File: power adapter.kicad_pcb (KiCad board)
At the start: 2 copper layers, 76.2 x 50.8 mm, 0 parts

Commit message: board started
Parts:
- added C3: T491C106M025AT7280, customfootprints:10uFtantcap, F.Cu at (38.7, 85.6)
- added C4: T491C106M025AT7280, customfootprints:10uFtantcap, F.Cu at (47.2, 99.4)
- added U1: ~, adapterpcblib:Header2x5, F.Cu at (40.4, 91.2)
- added jk1: ~, adapterpcblib:Banana, F.Cu at (81.5, 82.5)
- added jk2: ~, adapterpcblib:Banana, F.Cu at (80.8, 94.0)
- added jk3: ~, adapterpcblib:Banana, F.Cu at (80.0, 105.4)
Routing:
- net GND: track 0.00 -> 81.5 mm
- net -12V: track 0.00 -> 45.3 mm
- net +12V: track 0.00 -> 41.3 mm
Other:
- board size 76.2 x 50.8 mm -> 63.5 x 38.1 mm

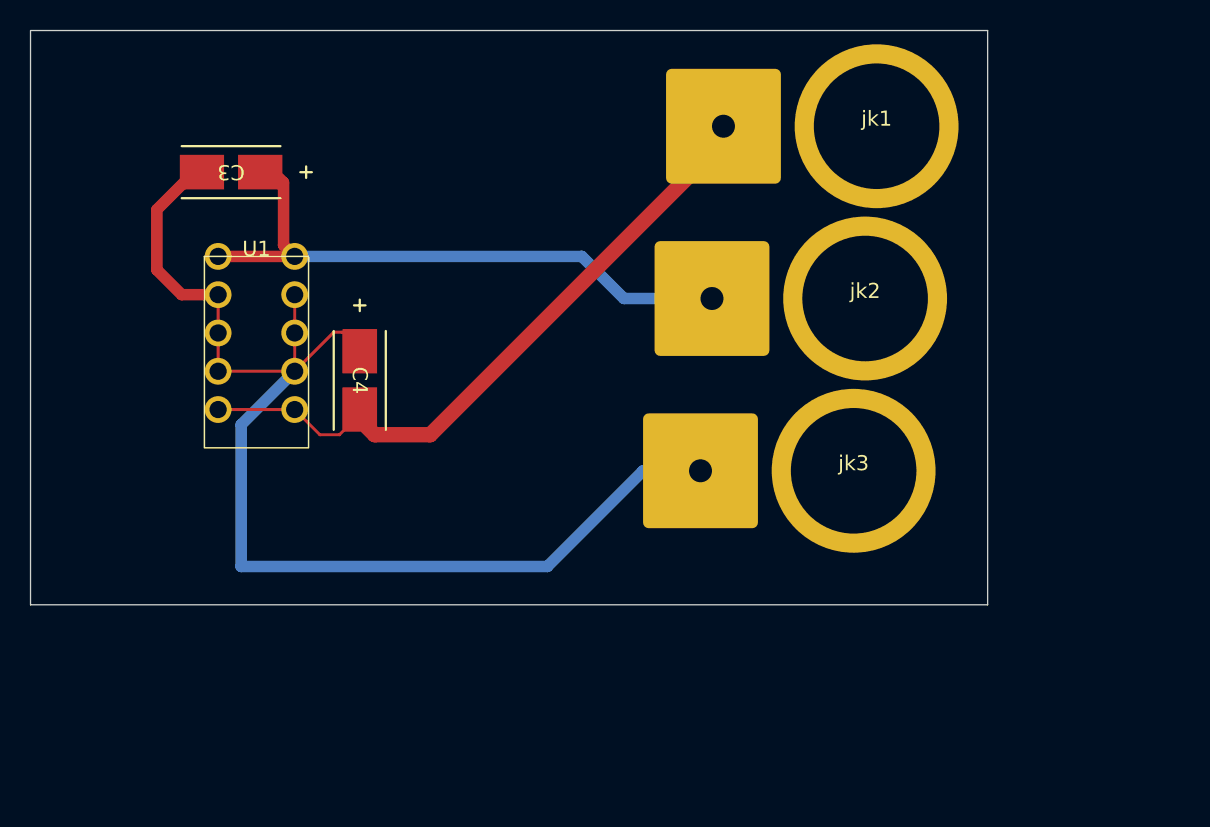
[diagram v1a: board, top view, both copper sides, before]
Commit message: rotated power header
rotated power header anotated schematic, turned on silkscreen layer
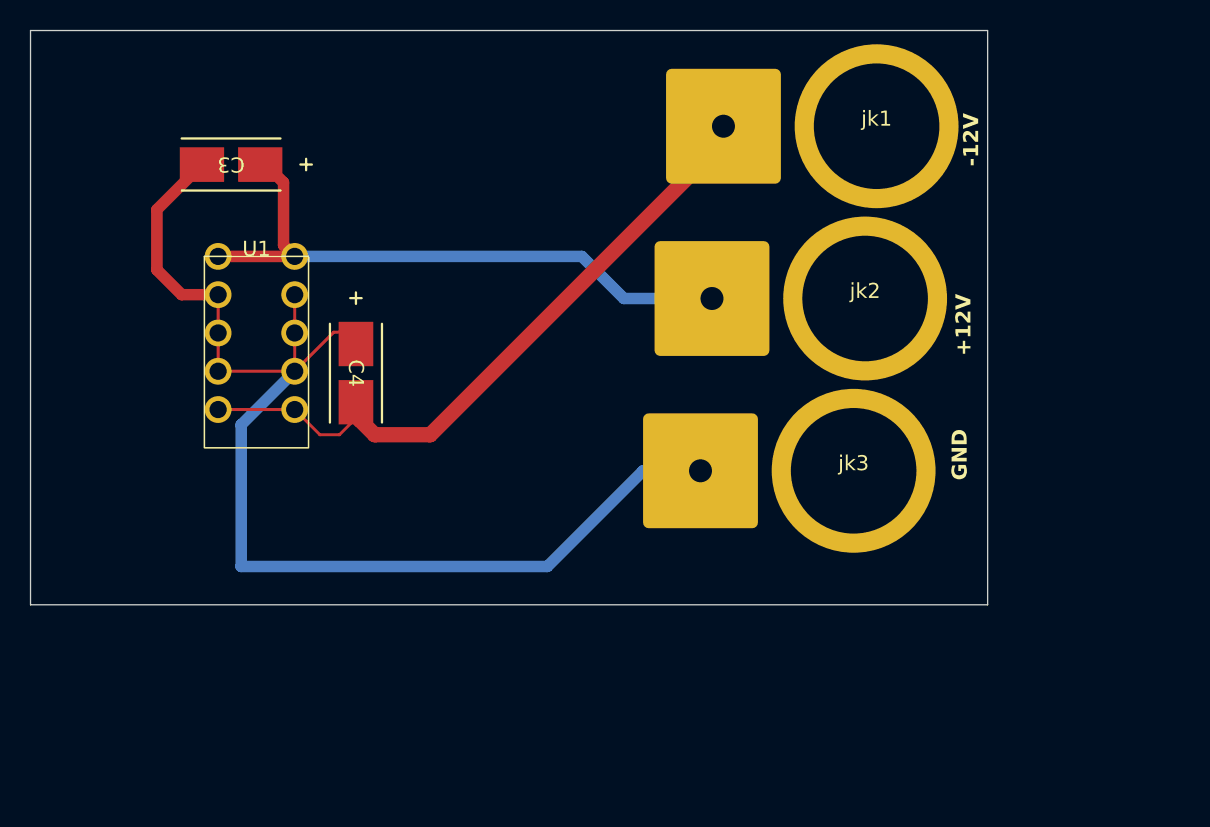
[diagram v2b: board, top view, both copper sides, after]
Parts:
- moved C4 0.54 mm to (47.0, 98.9)
- moved C3 0.51 mm to (38.7, 85.1)
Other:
- board text added: "+12V"
- board text added: "-12V"
- board text added: "GND"

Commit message: added power lanes
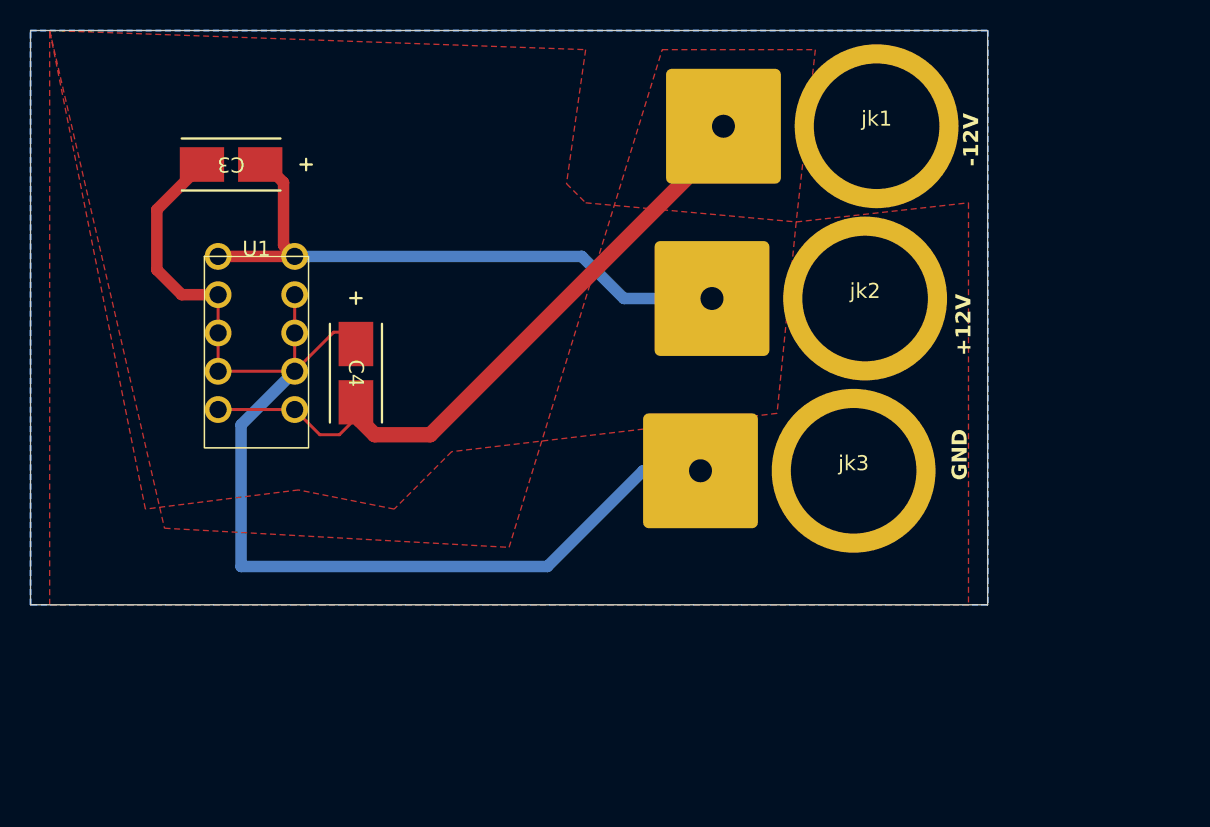
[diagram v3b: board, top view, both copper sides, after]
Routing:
- added copper zone on B.Cu, net (none)
- added copper zone on F.Cu, net +12V
- added copper zone on F.Cu, net -12V
- added copper zone on B.Cu, net GND

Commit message: updateEuroHeader
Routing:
- net GND: track 81.5 -> 82.3 mm, vias 0 -> 1
- removed copper zone on F.Cu, net +12V
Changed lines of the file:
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@@
 		(sheetfile "power adapter.kicad_sch")
 		(attr through_hole)
+		(fp_line
+			(start -4.525 -2.18)
+			(end 3.825 -2.18)
+			(stroke
+				(width 1.016)
+				(type default)
+			)
+			(layer "F.SilkS")
+		)
+		(fp_rect
+			(start -4.72 3.705)
+			(end -3.58 7.275)
+			(stroke
+				(width 0.1)
+				(type solid)
+			)
+			(fill solid)
+			(layer "F.SilkS")
+		)
 		(fp_rect
 			(start -3.45 0)
@@
 			)
 			(fill none)
+			(layer "F.SilkS")
+		)
+		(fp_circle
+			(center -4.37 0.01)
+			(end -3.93 0.01)
+			(stroke
+				(width 0.1)
+				(type solid)
+			)
+			(fill solid)
 			(layer "F.SilkS")
 		)
@@
 	)
 	(segment
-		(start 33.782 88.085492)
-		(end 33.782 92.075)
-		(width 0.762)
-		(layer "F.Cu")
-		(net 1)
-	)
-	(segment
 		(start 36.269492 85.598)
 		(end 36.773408 85.598)
@@
 	)
 	(segment
-		(start 33.782 92.075)
-		(end 35.433 93.726)
-		(width 0.762)
-		(layer "F.Cu")
-		(net 1)
-	)
-	(segment
-		(start 36.269492 85.598)
-		(end 33.782 88.085492)
-		(width 0.762)
-		(layer "F.Cu")
-		(net 1)
-	)
-	(segment
 		(start 45.51849 96.21351)
 		(end 46.084624 96.21351)
@@
 	)
 	(segment
-		(start 35.433 93.726)
-		(end 37.846 93.726)
-		(width 0.762)
+		(start 34.29 87.63)
+		(end 34.29 86.889886)
+		(width 1.016)
+		(layer "F.Cu")
+		(net 1)
+	)
+	(segment
+		(start 34.29 86.889886)
+		(end 36.089886 85.09)
+		(width 1.016)
 		(layer "F.Cu")
 		(net 1)
@@
 		(width 0.2)
 		(layer "F.Cu")
+		(net 1)
+	)
+	(segment
+		(start 36.089886 85.09)
+		(end 36.773408 85.09)
+		(width 1.016)
+		(layer "F.Cu")
+		(net 1)
+	)
+	(via
+		(at 34.29 87.63)
+		(size 0.5)
+		(drill 0.3)
+		(layers "F.Cu" "B.Cu")
 		(net 1)
 	)
@@
 	)
 	(segment
+		(start 35.306 93.726)
+		(end 34.29 92.71)
+		(width 1.016)
+		(layer "B.Cu")
+		(net 1)
+	)
+	(segment
 		(start 66.04 105.41)
 		(end 59.69 111.76)
@@
 	)
 	(segment
+		(start 37.846 93.726)
+		(end 35.306 93.726)
+		(width 1.016)
+		(layer "B.Cu")
+		(net 1)
+	)
+	(segment
 		(start 39.37 102.362)
 		(end 42.926 98.806)
 		(width 0.762)
+		(layer "B.Cu")
+		(net 1)
+	)
+	(segment
+		(start 34.29 92.71)
+		(end 34.29 87.63)
+		(width 1.016)
 		(layer "B.Cu")
 		(net 1)
@@
 	)
 	(zone
-		(net 3)
-		(net_name "+12V")
+		(net 2)
+		(net_name "-12V")
 		(layer "F.Cu")
 		(hatch edge 0.5)
-		(priority 4)
+		(priority 5)
 		(connect_pads
 			(clearance 0.5)
@@
 			(thermal_gap 0.5)
 			(thermal_bridge_width 0.5)
+			(island_removal_mode 1)
+			(island_area_min 9.999999)
 		)
 		(polygon
@@
 		(layer "F.Cu")
 		(hatch edge 0.5)
-		(priority 5)
+		(priority 4)
 		(connect_pads
 			(clearance 0.5)
@@
 		(polygon
 			(pts
-				(xy 26.67 76.2) (xy 34.29 109.22) (xy 57.15 110.49) (xy 67.31 77.47) (xy 77.47 77.47) (xy 76.2 88.9)
+				(xy 26.67 76.2) (xy 34.29 109.22) (xy 48.26 106.68) (xy 67.31 77.47) (xy 76.2 77.47) (xy 76.2 88.9)
 				(xy 87.63 87.63) (xy 87.63 114.3) (xy 26.67 114.3)
 			)
@@
 			(pts
 				(xy 25.4 76.2) (xy 88.9 76.2) (xy 88.9 114.3) (xy 25.4 114.3)
+			)
+		)
+	)
+	(zone
+		(net 1)
+		(net_name "GND")
+		(layer "B.Cu")
+		(hatch edge 0.5)
+		(priority 7)
+		(connect_pads
+			(clearance 0.5)
+		)
+		(min_thickness 0.25)
+		(filled_areas_thickness no)
+		(fill yes
+			(thermal_gap 0.5)
+			(thermal_bridge_width 0.5)
+			(island_removal_mode 1)
+			(island_area_min 9.999998)
+		)
+		(polygon
+			(pts
+				(xy 25.4 114.3) (xy 25.4 76.2) (xy 88.9 76.2) (xy 88.9 114.3)
 			)
 		)
@@
 			(thermal_bridge_width 0.5)
 			(island_removal_mode 1)
-			(island_area_min 9.999999)
+			(island_area_min 9.999998)
 		)
 		(polygon
 			(pts
-				(xy 88.9 76.2) (xy 88.9 114.3) (xy 25.4 114.3) (xy 25.4 76.2)
+				(xy 88.9 76.2) (xy 88.9 114.3) (xy 25.4 114.3)
 			)
 		)
@@
 			)
 		)
+	)
+	(zone
+		(net 1)
+		(net_name "GND")
+		(layer "B.Cu")
+		(hatch edge 0.5)
+		(priority 6)
+		(connect_pads
+			(clearance 0.5)
+		)
+		(min_thickness 0.25)
+		(filled_areas_thickness no)
+		(fill yes
+			(thermal_gap 0.5)
+			(thermal_bridge_width 0.5)
+			(island_removal_mode 1)
+			(island_area_min 9.999998)
+		)
+		(polygon
+			(pts
+				(xy 25.4 76.2) (xy 88.9 76.2) (xy 88.9 114.3) (xy 25.4 114.3)
+			)
+		)

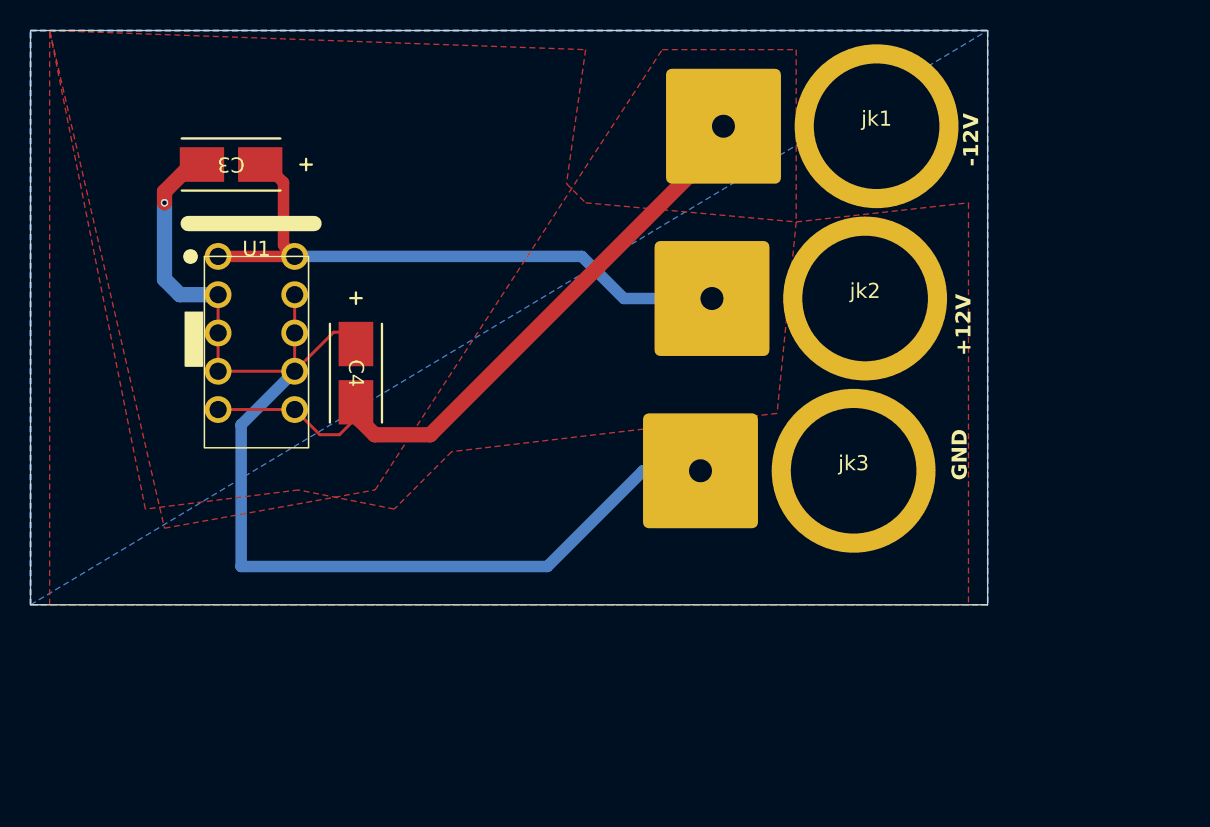
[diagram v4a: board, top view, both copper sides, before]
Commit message: better power planes
added better power planes and aded courtyards to a few footprints
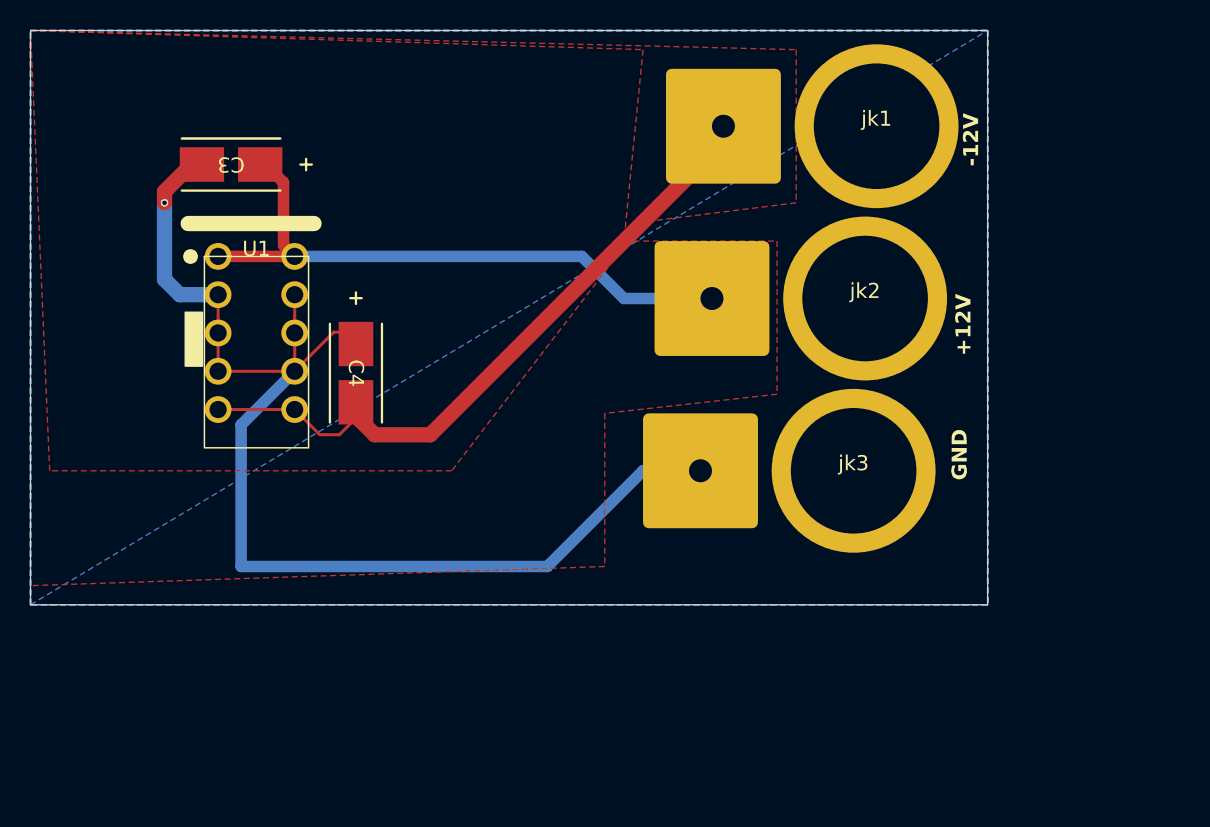
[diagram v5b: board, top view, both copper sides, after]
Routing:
- added copper zone on B.Cu, net +12V
- added copper zone on F.Cu, net +12V
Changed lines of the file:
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@@
 		(sheetfile "power adapter.kicad_sch")
 		(attr through_hole)
+		(fp_rect
+			(start -14.89 -5.39)
+			(end 5.36 5.64)
+			(stroke
+				(width 0.05)
+				(type solid)
+			)
+			(fill solid)
+			(layer "F.CrtYd")
+		)
 		(fp_text user "${REFERENCE}"
 			(at 0 2.5 0)
@@
 		(sheetfile "power adapter.kicad_sch")
 		(attr through_hole)
+		(fp_rect
+			(start -14.89 -5.39)
+			(end 5.36 5.64)
+			(stroke
+				(width 0.05)
+				(type solid)
+			)
+			(fill solid)
+			(layer "F.CrtYd")
+		)
 		(fp_text user "${REFERENCE}"
 			(at 0 2.5 0)
@@
 		(sheetfile "power adapter.kicad_sch")
 		(attr through_hole)
+		(fp_rect
+			(start -14.89 -5.39)
+			(end 5.36 5.64)
+			(stroke
+				(width 0.05)
+				(type solid)
+			)
+			(fill solid)
+			(layer "F.CrtYd")
+		)
 		(fp_text user "${REFERENCE}"
 			(at 0 2.5 0)
@@
 	)
 	(zone
+		(net 3)
+		(net_name "+12V")
+		(layer "F.Cu")
+		(hatch edge 0.5)
+		(priority 4)
+		(connect_pads
+			(clearance 0.5)
+		)
+		(min_thickness 0.25)
+		(filled_areas_thickness no)
+		(fill yes
+			(thermal_gap 0.5)
+			(thermal_bridge_width 0.5)
+		)
+		(polygon
+			(pts
+				(xy 25.4 76.2) (xy 66.04 77.47) (xy 64.77 90.17) (xy 74.93 90.17) (xy 74.93 100.33) (xy 63.5 101.6)
+				(xy 63.5 111.76) (xy 25.4 113.03)
+			)
+		)
+	)
+	(zone
 		(net 2)
 		(net_name "-12V")
@@
 		(hatch edge 0.5)
 		(priority 5)
+		(connect_pads
+			(clearance 0.5)
+		)
+		(min_thickness 0.25)
+		(filled_areas_thickness no)
+		(fill yes
+			(thermal_gap 0.5)
+			(thermal_bridge_width 0.5)
+		)
+		(polygon
+			(pts
+				(xy 25.4 76.2) (xy 76.2 77.47) (xy 76.2 87.63) (xy 66.04 88.9) (xy 53.34 105.41) (xy 26.67 105.41)
+			)
+		)
+	)
+	(zone
+		(net 1)
+		(net_name "GND")
+		(layer "B.Cu")
+		(hatch edge 0.5)
+		(connect_pads
+			(clearance 0.5)
+		)
+		(min_thickness 0.25)
+		(filled_areas_thickness no)
+		(fill yes
+			(thermal_gap 0.5)
+			(thermal_bridge_width 0.5)
+		)
+		(polygon
+			(pts
+				(xy 25.4 76.2) (xy 88.9 76.2) (xy 88.9 114.3) (xy 25.4 114.3)
+			)
+		)
+	)
+	(zone
+		(net 1)
+		(net_name "GND")
+		(layer "B.Cu")
+		(hatch edge 0.5)
+		(priority 2)
+		(connect_pads
+			(clearance 0.5)
+		)
+		(min_thickness 0.25)
+		(filled_areas_thickness no)
+		(fill yes
+			(thermal_gap 0.5)
+			(thermal_bridge_width 0.5)
+		)
+		(polygon
+			(pts
+				(xy 25.4 76.2) (xy 88.9 76.2) (xy 88.9 114.3) (xy 25.4 114.3)
+			)
+		)
+	)
+	(zone
+		(net 3)
+		(net_name "+12V")
+		(layer "B.Cu")
+		(hatch edge 0.5)
+		(priority 7)
 		(connect_pads
 			(clearance 0.5)
@@
 			(thermal_bridge_width 0.5)
 			(island_removal_mode 1)
-			(island_area_min 9.999999)
+			(island_area_min 9.999997)
 		)
 		(polygon
-			(pts
-				(xy 26.67 76.2) (xy 62.23 77.47) (xy 60.96 86.36) (xy 62.23 87.63) (xy 76.2 88.9) (xy 74.93 101.6)
-				(xy 53.34 104.14) (xy 49.53 107.95) (xy 43.18 106.68) (xy 33.02 107.95)
-			)
-		)
-	)
-	(zone
-		(net 2)
-		(net_name "-12V")
-		(layer "F.Cu")
-		(hatch edge 0.5)
-		(priority 4)
-		(connect_pads
-			(clearance 0.5)
-		)
-		(min_thickness 0.25)
-		(filled_areas_thickness no)
-		(fill yes
-			(thermal_gap 0.5)
-			(thermal_bridge_width 0.5)
-		)
-		(polygon
-			(pts
-				(xy 26.67 76.2) (xy 34.29 109.22) (xy 48.26 106.68) (xy 67.31 77.47) (xy 76.2 77.47) (xy 76.2 88.9)
-				(xy 87.63 87.63) (xy 87.63 114.3) (xy 26.67 114.3)
-			)
-		)
-	)
-	(zone
-		(net 1)
-		(net_name "GND")
-		(layer "B.Cu")
-		(hatch edge 0.5)
-		(connect_pads
-			(clearance 0.5)
-		)
-		(min_thickness 0.25)
-		(filled_areas_thickness no)
-		(fill yes
-			(thermal_gap 0.5)
-			(thermal_bridge_width 0.5)
-		)
-		(polygon
-			(pts
-				(xy 25.4 76.2) (xy 88.9 76.2) (xy 88.9 114.3) (xy 25.4 114.3)
-			)
-		)
-	)
-	(zone
-		(net 1)
-		(net_name "GND")
-		(layer "B.Cu")
-		(hatch edge 0.5)
-		(priority 2)
-		(connect_pads
-			(clearance 0.5)
-		)
-		(min_thickness 0.25)
-		(filled_areas_thickness no)
-		(fill yes
-			(thermal_gap 0.5)
-			(thermal_bridge_width 0.5)
-		)
-		(polygon
-			(pts
-				(xy 25.4 76.2) (xy 88.9 76.2) (xy 88.9 114.3) (xy 25.4 114.3)
-			)
-		)
-	)
-	(zone
-		(net 1)
-		(net_name "GND")
-		(layer "B.Cu")
-		(hatch edge 0.5)
-		(priority 7)
-		(connect_pads
-			(clearance 0.5)
-		)
-		(min_thickness 0.25)
-		(filled_areas_thickness no)
-		(fill yes
-			(thermal_gap 0.5)
-			(thermal_bridge_width 0.5)
-			(island_removal_mode 1)
-			(island_area_min 9.999998)
-		)
-		(polygon
